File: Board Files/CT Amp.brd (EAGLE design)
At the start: 47.9 x 41.3 mm, 42 parts, among them IC1 LM324N

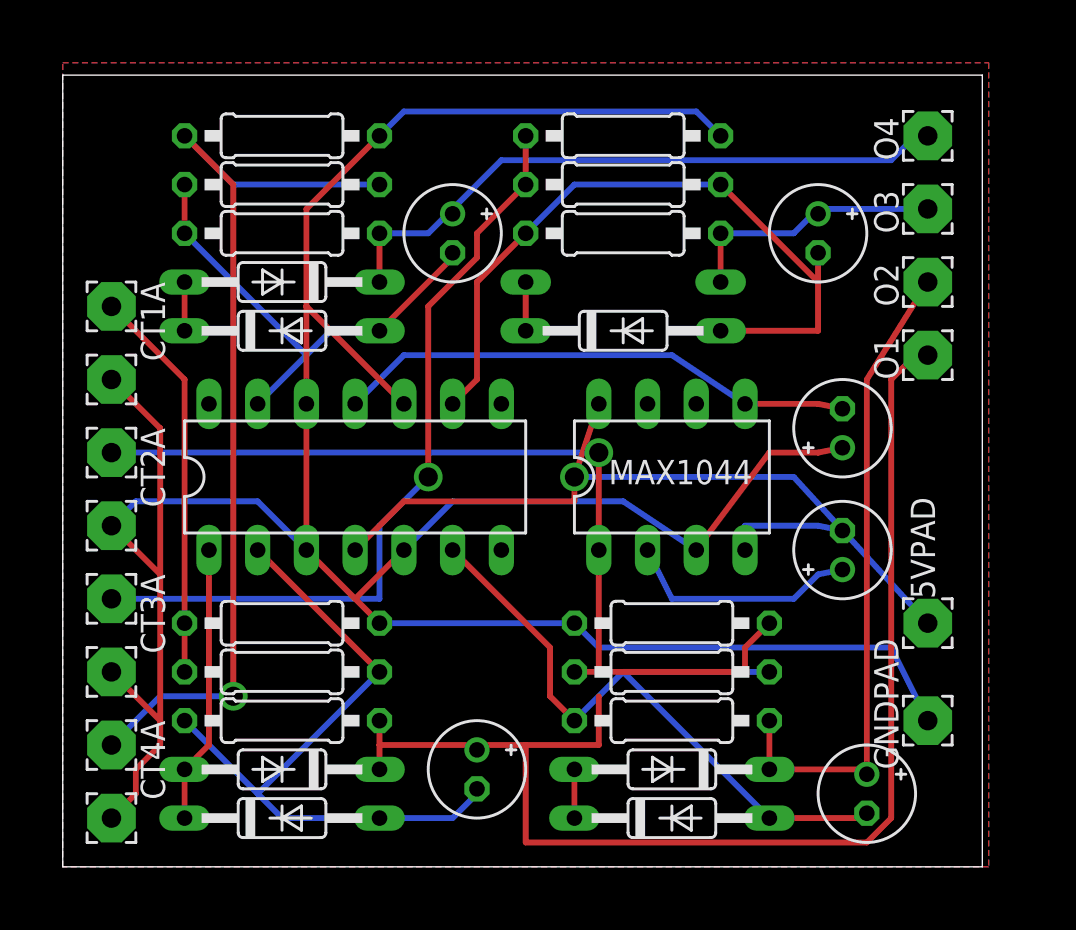
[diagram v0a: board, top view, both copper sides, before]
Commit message: v2 - Rerouted PCB
Original board had some problems, so I rerouted the traces
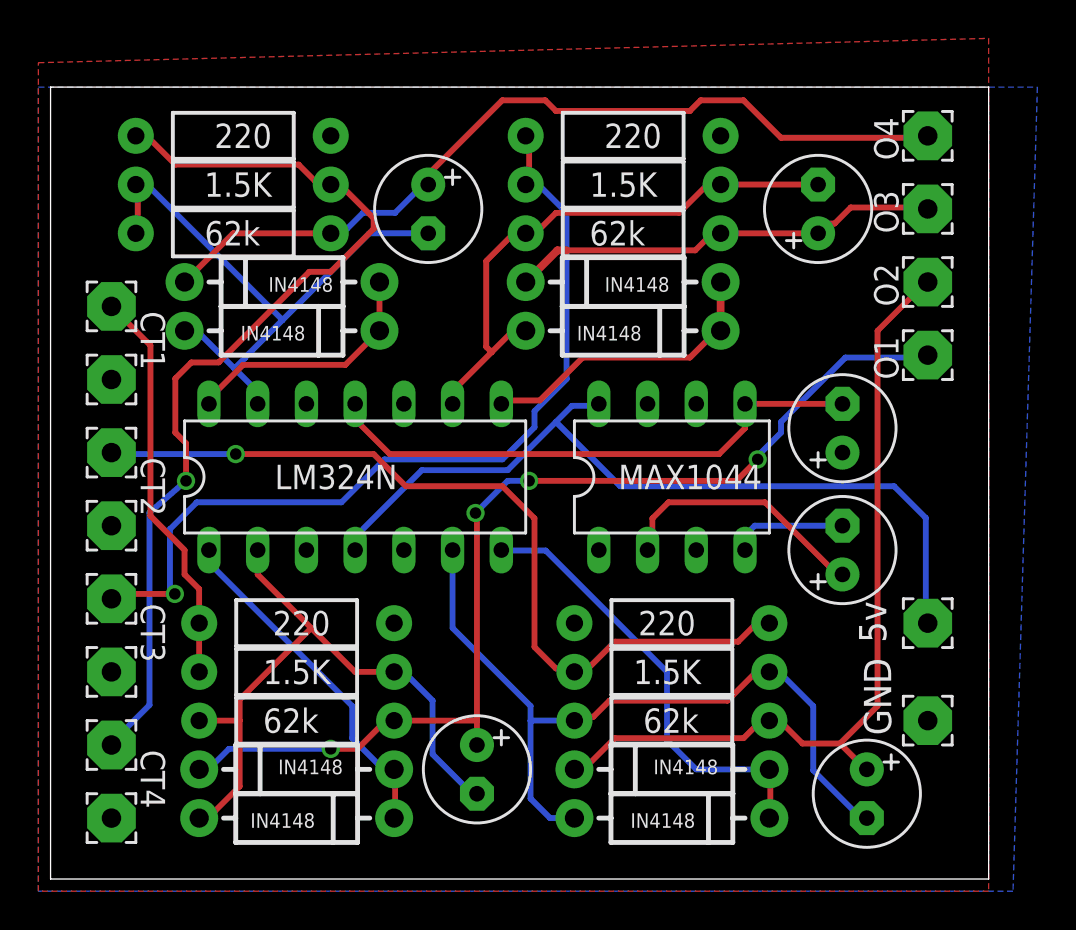
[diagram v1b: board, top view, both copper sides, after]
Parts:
- C1, C2, C3, C4, C5, C6: device resistor:E2-5 -> adafruit:E2,5-6
- D1, D2, D3, D4, D5, D6, D7, D8: value 1N4148DO35-10 -> IN4148; device diode:DO35-10 -> SparkFun-DiscreteSemi:DIODE-1N4001
- R1, R10, R11, R12, R2, R3, R4, R5, R6, R7, R8, R9: device resistor:0207/10 -> SparkFun-Resistors:AXIAL-0.4
- moved R10 2.54 mm to (8.89, 35.6)
- moved R11 2.54 mm to (8.89, 38.1)
- moved R12 2.54 mm to (8.89, 33.0)
- moved C6 1.80 mm to (19.1, 34.3)
- moved C5 1.27 mm to (39.4, 34.3), turned to 90 degrees
- moved D1 0.76 mm to (12.2, 5.08)
- moved D2 0.76 mm to (12.2, 2.54)
- moved R1 0.76 mm to (12.2, 10.2)
- moved R2 0.76 mm to (12.2, 12.7)
- moved R3 0.76 mm to (12.2, 7.62)
- flipped D5 to the top, turned to 180 degrees
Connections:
- net GND: now also R11.P$1, R2.P$1, R5.P$1, R8.P$1; no longer R11.1, R2.1, R5.1, R8.1
- net N$10: now also R9.P$2; no longer R9.2
- net N$11: now also R10.P$2, R12.P$1; no longer R10.2, R12.1
- net N$12: now also R4.P$2, R6.P$1; no longer R4.2, R6.1
- net N$13: now also IC1.14
- net N$14: now also R12.P$2; no longer R12.2
- net N$16: now also R3.P$2; no longer R3.2
- net N$17: now also R1.P$1, R2.P$2; no longer R1.1, R2.2
- net N$20: now also R10.P$1, R11.P$2; no longer R10.1, R11.2
- net N$21: now also IC1.7
- net N$22: now also R6.P$2; no longer R6.2
- net N$3: now also R4.P$1, R5.P$2; no longer R4.1, R5.2
- net N$4: now also R1.P$2, R3.P$1; no longer R1.2, R3.1
- net N$5: now also R7.P$2, R9.P$1; no longer R7.2, R9.1
- net N$6: now also R7.P$1, R8.P$2; no longer R7.1, R8.2
- net N$9: now also IC1.8
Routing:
- net GND: track 160.8 -> 0.00 mm
- net N$21: track 2.54 -> 23.3 mm
- net N$9: track 2.54 -> 15.7 mm
- net N$14: track 33.5 -> 44.8 mm
- net N$16: track 66.7 -> 55.6 mm, vias 0 -> 4
- net N$13: track 2.54 -> 13.2 mm
- net N$22: track 34.2 -> 43.6 mm
- net N$10: track 14.1 -> 23.1 mm
- net N$5: track 38.0 -> 29.6 mm
- net N$11: track 25.1 -> 32.3 mm
- net N$3: track 48.8 -> 44.0 mm
- net N$6: track 41.3 -> 45.4 mm
- net N$8: track 14.5 -> 18.4 mm
- net +5V: track 39.5 -> 43.2 mm, vias 1 -> 0
- net N$12: track 38.8 -> 41.0 mm
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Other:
- board size 47.9 x 41.3 mm -> 48.9 x 41.3 mm
- board text added: "5v"
- board text added: "CT1"
- board text added: "CT2"
- board text added: "CT3"
- board text added: "CT4"
- board text added: "Current Sensor v2.0"
- board text added: "GND"
